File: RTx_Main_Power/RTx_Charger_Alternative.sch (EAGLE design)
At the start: 9 parts, among them IC1 TL331, Q1 STW11NM80

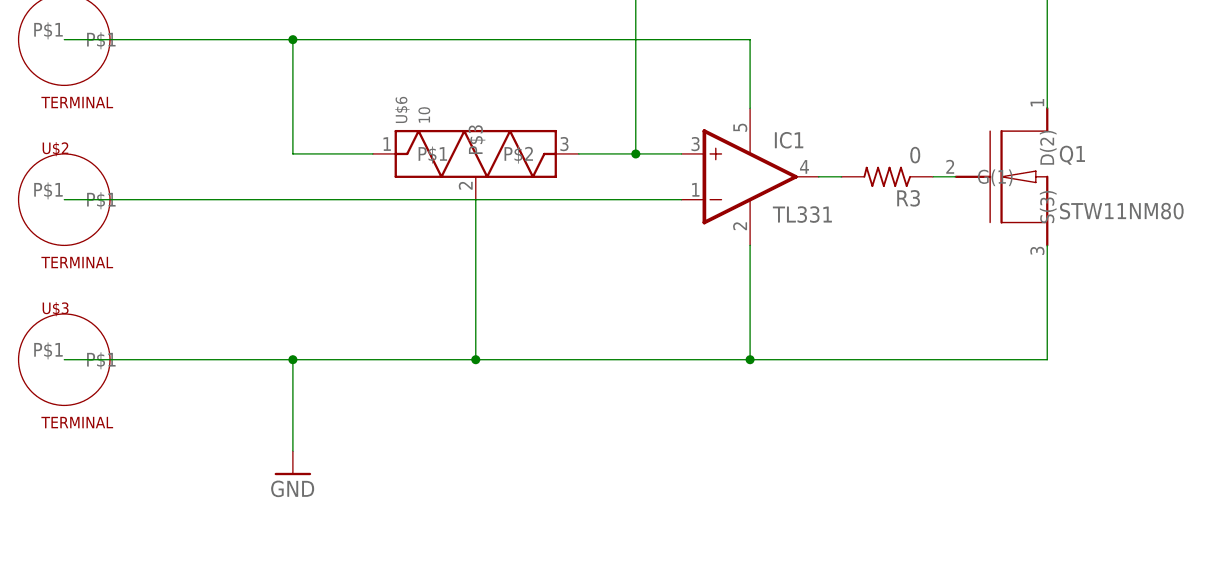
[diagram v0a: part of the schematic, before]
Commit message: Added voltage divider to inverting input of opamp.
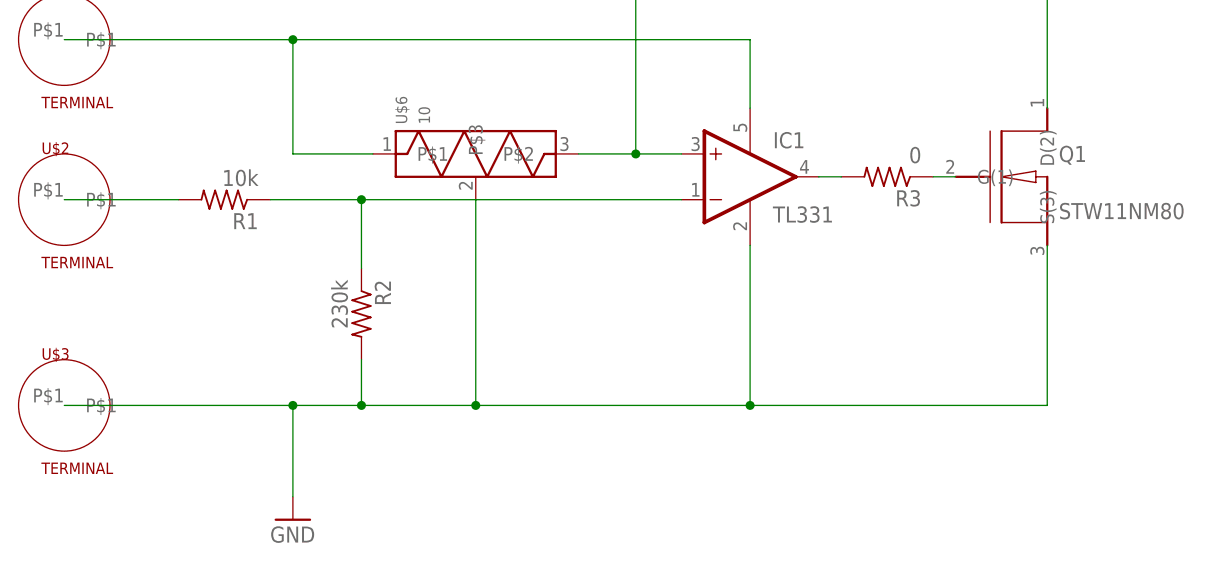
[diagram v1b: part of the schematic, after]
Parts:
- added R1: 10k, motorFeedback:R-US_R1206
- added R2: 230k, motorFeedback:R-US_R1206
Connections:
- new net N$7: R1.2, U$2.P$1
- net GND: now also R2.2
- net N$6: now also R1.1, R2.1; no longer U$2.P$1
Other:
- moved on the sheet: U$3
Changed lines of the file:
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@@
 <part name="U$5" library="temp_library" deviceset="TERMINAL" device=""/>
 <part name="U$7" library="temp_library" deviceset="TERMINAL" device=""/>
+<part name="R1" library="motorFeedback" deviceset="R-US_" device="R1206" value="10k"/>
+<part name="R2" library="motorFeedback" deviceset="R-US_" device="R1206" value="230k"/>
 </parts>
 <sheets>
@@
 <instance part="R3" gate="G$1" x="200.66" y="91.44" rot="R180"/>
 <instance part="Q1" gate="G$1" x="210.82" y="99.06"/>
-<instance part="GND1" gate="1" x="134.62" y="58.42"/>
+<instance part="GND1" gate="1" x="134.62" y="53.34"/>
 <instance part="U$6" gate="G$1" x="154.94" y="93.98" rot="R90"/>
 <instance part="U$2" gate="G$1" x="109.22" y="88.9"/>
-<instance part="U$3" gate="G$1" x="109.22" y="71.12"/>
+<instance part="U$3" gate="G$1" x="109.22" y="66.04"/>
 <instance part="U$4" gate="G$1" x="109.22" y="106.68"/>
 <instance part="U$5" gate="G$1" x="218.44" y="121.92"/>
 <instance part="U$7" gate="G$1" x="172.72" y="121.92"/>
+<instance part="R1" gate="G$1" x="127" y="88.9" rot="R180"/>
+<instance part="R2" gate="G$1" x="142.24" y="76.2" rot="R270"/>
 </instances>
 <busses>
@@
 <segment>
 <pinref part="IC1" gate="G$1" pin="-IN"/>
-<wire x1="177.8" y1="88.9" x2="109.22" y2="88.9" width="0.1524" layer="91"/>
-<pinref part="U$2" gate="G$1" pin="P$1"/>
+<wire x1="177.8" y1="88.9" x2="142.24" y2="88.9" width="0.1524" layer="91"/>
+<pinref part="R1" gate="G$1" pin="1"/>
+<pinref part="R2" gate="G$1" pin="1"/>
+<wire x1="142.24" y1="88.9" x2="132.08" y2="88.9" width="0.1524" layer="91"/>
+<wire x1="142.24" y1="81.28" x2="142.24" y2="88.9" width="0.1524" layer="91"/>
+<junction x="142.24" y="88.9"/>
 </segment>
 </net>
@@
 <segment>
 <pinref part="IC1" gate="G$1" pin="GND"/>
-<wire x1="185.42" y1="83.82" x2="185.42" y2="71.12" width="0.1524" layer="91"/>
-<wire x1="185.42" y1="71.12" x2="154.94" y2="71.12" width="0.1524" layer="91"/>
-<junction x="185.42" y="71.12"/>
-<wire x1="218.44" y1="71.12" x2="185.42" y2="71.12" width="0.1524" layer="91"/>
+<wire x1="185.42" y1="83.82" x2="185.42" y2="66.04" width="0.1524" layer="91"/>
+<wire x1="185.42" y1="66.04" x2="154.94" y2="66.04" width="0.1524" layer="91"/>
+<junction x="185.42" y="66.04"/>
+<wire x1="218.44" y1="66.04" x2="185.42" y2="66.04" width="0.1524" layer="91"/>
 <pinref part="Q1" gate="G$1" pin="S(3)"/>
-<wire x1="218.44" y1="83.82" x2="218.44" y2="71.12" width="0.1524" layer="91"/>
+<wire x1="218.44" y1="83.82" x2="218.44" y2="66.04" width="0.1524" layer="91"/>
 <pinref part="U$6" gate="G$1" pin="P$3"/>
-<wire x1="154.94" y1="88.9" x2="154.94" y2="71.12" width="0.1524" layer="91"/>
-<junction x="154.94" y="71.12"/>
+<wire x1="154.94" y1="88.9" x2="154.94" y2="66.04" width="0.1524" layer="91"/>
+<junction x="154.94" y="66.04"/>
 <pinref part="U$3" gate="G$1" pin="P$1"/>
-<wire x1="154.94" y1="71.12" x2="134.62" y2="71.12" width="0.1524" layer="91"/>
+<wire x1="154.94" y1="66.04" x2="142.24" y2="66.04" width="0.1524" layer="91"/>
 <pinref part="GND1" gate="1" pin="GND"/>
-<wire x1="134.62" y1="71.12" x2="109.22" y2="71.12" width="0.1524" layer="91"/>
-<wire x1="134.62" y1="60.96" x2="134.62" y2="71.12" width="0.1524" layer="91"/>
-<junction x="134.62" y="71.12"/>
+<wire x1="142.24" y1="66.04" x2="134.62" y2="66.04" width="0.1524" layer="91"/>
+<wire x1="134.62" y1="66.04" x2="109.22" y2="66.04" width="0.1524" layer="91"/>
+<wire x1="134.62" y1="55.88" x2="134.62" y2="66.04" width="0.1524" layer="91"/>
+<junction x="134.62" y="66.04"/>
+<pinref part="R2" gate="G$1" pin="2"/>
+<wire x1="142.24" y1="66.04" x2="142.24" y2="71.12" width="0.1524" layer="91"/>
+<junction x="142.24" y="66.04"/>
 </segment>
 </net>
+<net name="N$7" class="0">
+<segment>
+<pinref part="U$2" gate="G$1" pin="P$1"/>
+<pinref part="R1" gate="G$1" pin="2"/>
+<wire x1="121.92" y1="88.9" x2="109.22" y2="88.9" width="0.1524" layer="91"/>
+</segment>
+</net>

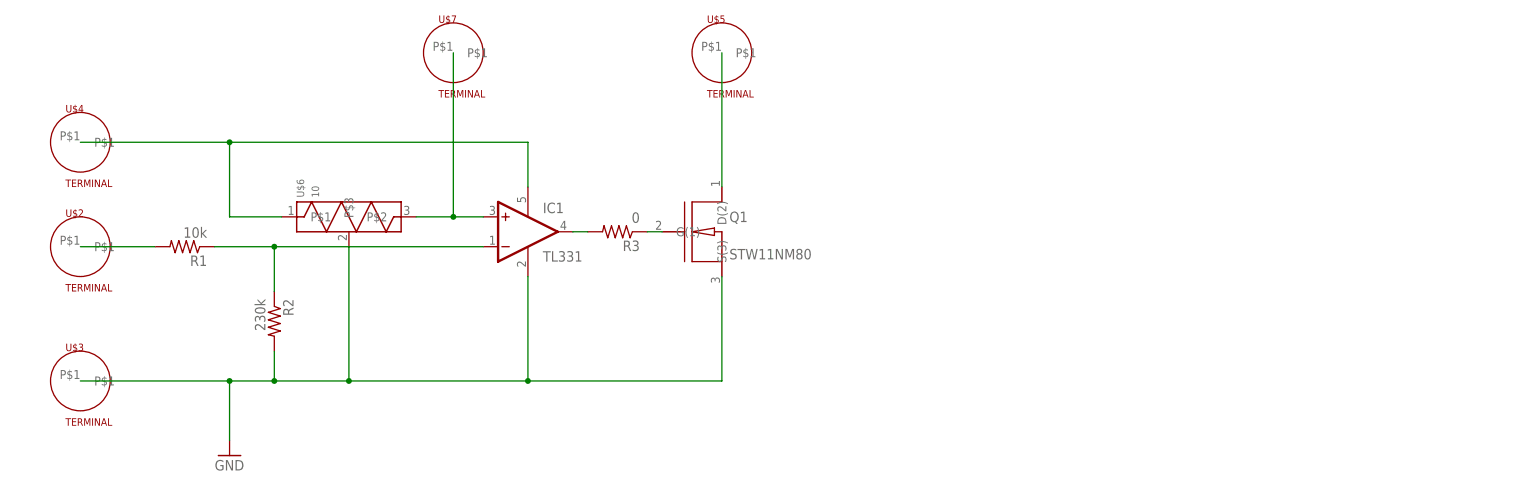
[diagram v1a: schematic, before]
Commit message: Updated controller schematic with high speed signal routing information. Added termination resistor to SPI_SCK line. Included Sightline documentation. Added avionics library, node4-2.lbr, to RTx controller library folder. Made progress on RTx_Charger board layout.
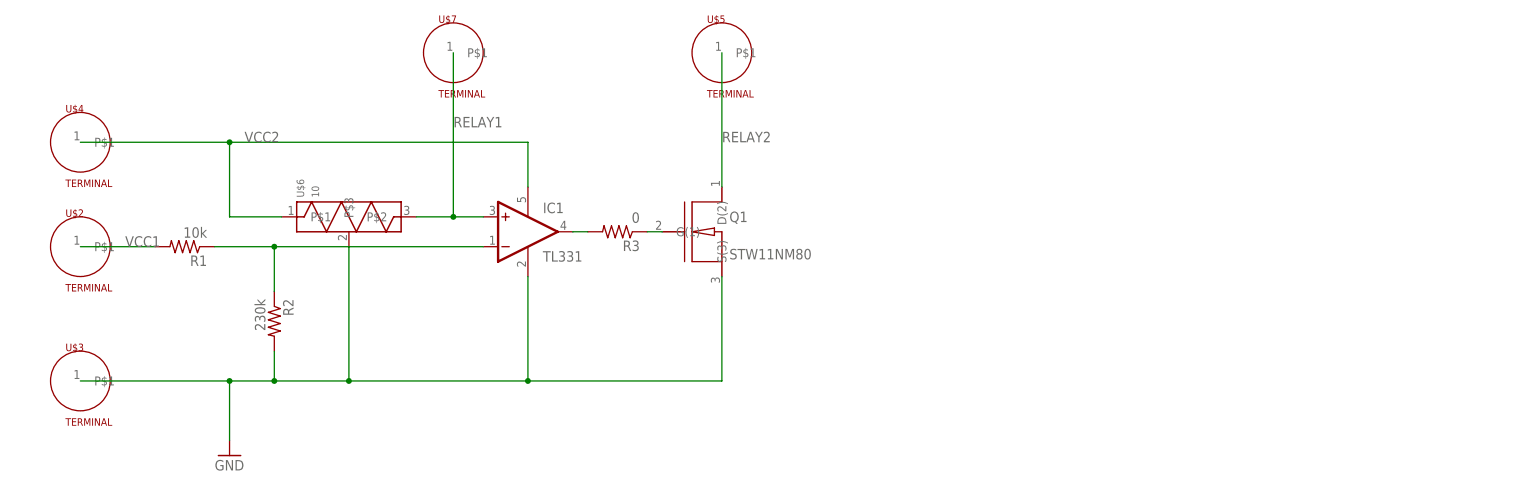
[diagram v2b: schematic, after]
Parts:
- U$2, U$3, U$4, U$5, U$7: device temp_library:TERMINAL -> temp_library:TERMINAL_BATTERY
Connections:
- net N$2 renamed VCC2
- net N$4 renamed RELAY2
- net N$7 renamed VCC1
- removed net N$3: U$6.P$2, U$7.P$1
- new net RELAY1: IC1.+IN, U$6.P$2, U$7.P$1
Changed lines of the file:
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@@
 <part name="GND1" library="motorFeedback" deviceset="GND" device=""/>
 <part name="U$6" library="temp_library" deviceset="TEH70" device="" value="10"/>
-<part name="U$2" library="temp_library" deviceset="TERMINAL" device=""/>
-<part name="U$3" library="temp_library" deviceset="TERMINAL" device=""/>
-<part name="U$4" library="temp_library" deviceset="TERMINAL" device=""/>
-<part name="U$5" library="temp_library" deviceset="TERMINAL" device=""/>
-<part name="U$7" library="temp_library" deviceset="TERMINAL" device=""/>
+<part name="U$2" library="temp_library" deviceset="TERMINAL_BATTERY" device="" value="TERMINAL"/>
+<part name="U$3" library="temp_library" deviceset="TERMINAL_BATTERY" device="" value="TERMINAL"/>
+<part name="U$4" library="temp_library" deviceset="TERMINAL_BATTERY" device="" value="TERMINAL"/>
+<part name="U$5" library="temp_library" deviceset="TERMINAL_BATTERY" device="" value="TERMINAL"/>
+<part name="U$7" library="temp_library" deviceset="TERMINAL_BATTERY" device="" value="TERMINAL"/>
 <part name="R1" library="motorFeedback" deviceset="R-US_" device="R1206" value="10k"/>
 <part name="R2" library="motorFeedback" deviceset="R-US_" device="R1206" value="230k"/>
@@
 </segment>
 </net>
-<net name="N$2" class="0">
+<net name="VCC2" class="0">
 <segment>
 <wire x1="134.62" y1="93.98" x2="143.51" y2="93.98" width="0.1524" layer="91"/>
@@
 <wire x1="134.62" y1="93.98" x2="134.62" y2="106.68" width="0.1524" layer="91"/>
 <junction x="134.62" y="106.68"/>
+<label x="137.16" y="106.68" size="1.778" layer="95"/>
 </segment>
 </net>
-<net name="N$3" class="0">
+<net name="RELAY1" class="0">
 <segment>
 <wire x1="166.37" y1="93.98" x2="172.72" y2="93.98" width="0.1524" layer="91"/>
-<wire x1="172.72" y1="93.98" x2="177.8" y2="93.98" width="0.1524" layer="91"/>
 <wire x1="172.72" y1="93.98" x2="172.72" y2="121.92" width="0.1524" layer="91"/>
-<junction x="172.72" y="93.98"/>
 <pinref part="U$6" gate="G$1" pin="P$2"/>
 <pinref part="U$7" gate="G$1" pin="P$1"/>
+<label x="172.72" y="109.22" size="1.778" layer="95"/>
+<pinref part="IC1" gate="G$1" pin="+IN"/>
+<wire x1="177.8" y1="93.98" x2="172.72" y2="93.98" width="0.1524" layer="91"/>
+<junction x="172.72" y="93.98"/>
 </segment>
 </net>
-<net name="N$4" class="0">
+<net name="RELAY2" class="0">
 <segment>
 <pinref part="Q1" gate="G$1" pin="D(2)"/>
 <wire x1="218.44" y1="99.06" x2="218.44" y2="121.92" width="0.1524" layer="91"/>
 <pinref part="U$5" gate="G$1" pin="P$1"/>
+<label x="218.44" y="106.68" size="1.778" layer="95"/>
 </segment>
 </net>
@@
 <wire x1="154.94" y1="88.9" x2="154.94" y2="66.04" width="0.1524" layer="91"/>
 <junction x="154.94" y="66.04"/>
-<pinref part="U$3" gate="G$1" pin="P$1"/>
 <wire x1="154.94" y1="66.04" x2="142.24" y2="66.04" width="0.1524" layer="91"/>
 <pinref part="GND1" gate="1" pin="GND"/>
 <wire x1="142.24" y1="66.04" x2="134.62" y2="66.04" width="0.1524" layer="91"/>
-<wire x1="134.62" y1="66.04" x2="109.22" y2="66.04" width="0.1524" layer="91"/>
 <wire x1="134.62" y1="55.88" x2="134.62" y2="66.04" width="0.1524" layer="91"/>
-<junction x="134.62" y="66.04"/>
 <pinref part="R2" gate="G$1" pin="2"/>
 <wire x1="142.24" y1="66.04" x2="142.24" y2="71.12" width="0.1524" layer="91"/>
 <junction x="142.24" y="66.04"/>
+<pinref part="U$3" gate="G$1" pin="P$1"/>
+<wire x1="134.62" y1="66.04" x2="109.22" y2="66.04" width="0.1524" layer="91"/>
+<junction x="134.62" y="66.04"/>
 </segment>
 </net>
-<net name="N$7" class="0">
+<net name="VCC1" class="0">
 <segment>
 <pinref part="U$2" gate="G$1" pin="P$1"/>
 <pinref part="R1" gate="G$1" pin="2"/>
 <wire x1="121.92" y1="88.9" x2="109.22" y2="88.9" width="0.1524" layer="91"/>
+<label x="116.84" y="88.9" size="1.778" layer="95"/>
 </segment>
 </net>
